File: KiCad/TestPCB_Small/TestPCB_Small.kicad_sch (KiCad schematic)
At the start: 82 parts, among them J2 USB4135-GF-A, Q1 SFH_3711, Q2 2N7002, Q3 2N7002, U1 ESP32-S3-WROOM-1, U1 MCP73831-2-OT, U2 TC1185-xCT, U4 LSM6DSM

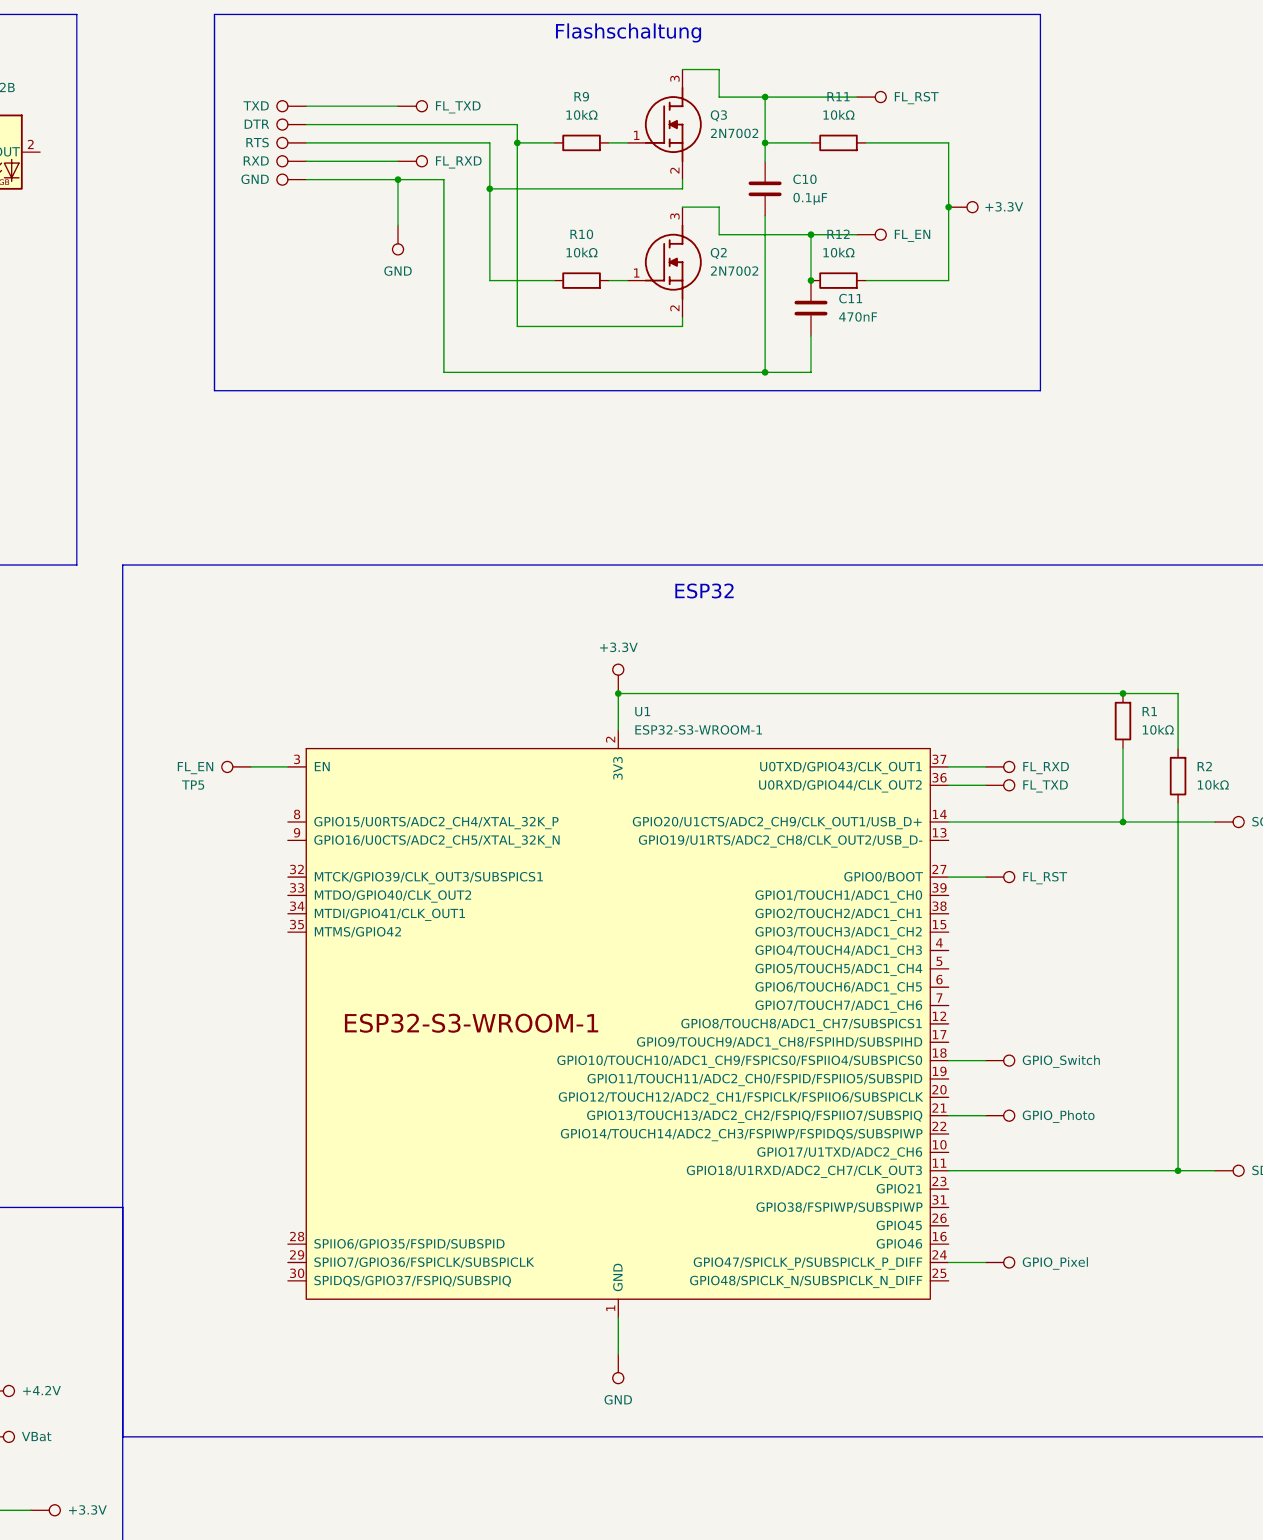
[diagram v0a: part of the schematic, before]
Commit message: CHG: pcb-layouts adopted
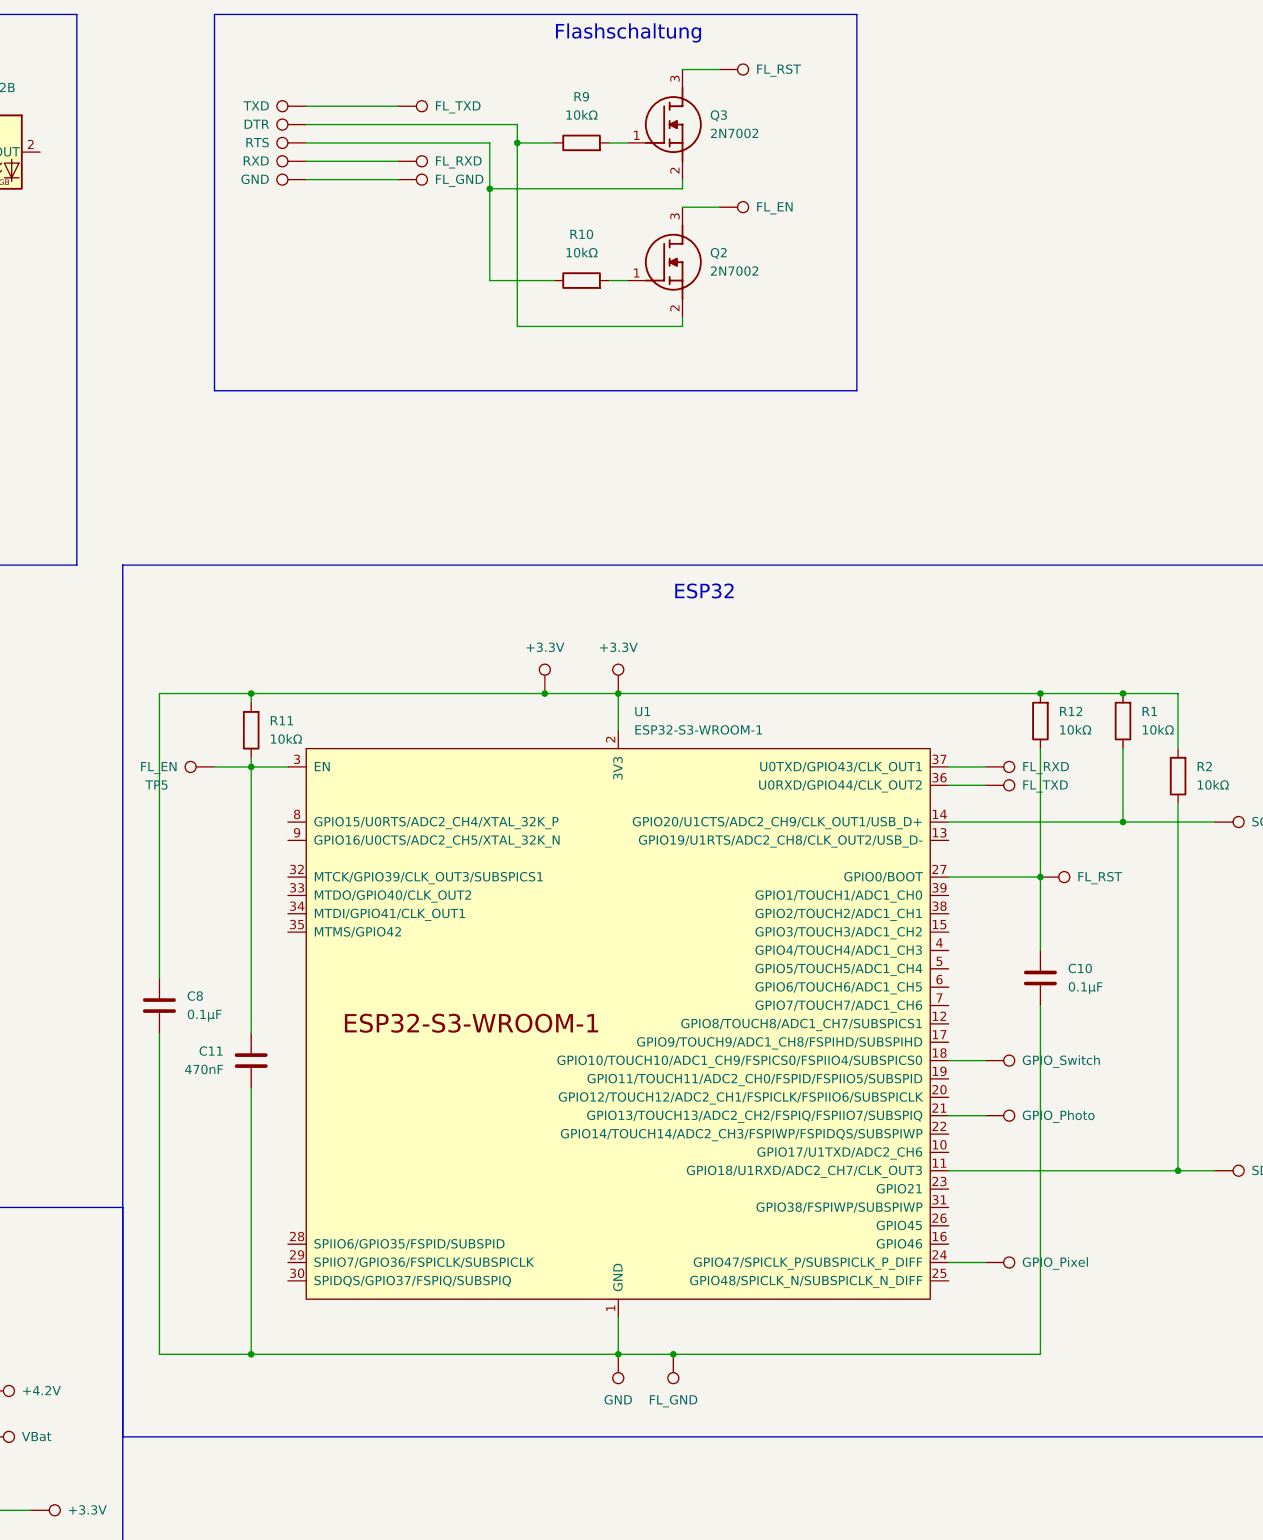
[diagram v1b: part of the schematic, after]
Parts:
- added C8: 0.1µF, Capacitor_SMD:C_0805_2012Metric, symbol Device:C
- added TP39: +3.3V, TestPoint:TestPoint_Pad_2.0x2.0mm, symbol Connector:TestPoint
- TP13: value GND -> FL_GND
- TP7: value +3.3V -> FL_GND
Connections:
- net at R11.2, R12.2: now also R1.2, R2.2, TP1.1, U1.2 (3V3), C8.1, TP39.1; no longer TP7.1
- net at Q2.3 (D), TP14.1: no longer C11.1, R12.1
- net at TP12.1, TP13.1: no longer C10.2, C11.2
- net at Q3.3 (D), TP17.1: no longer C10.1, R11.1
- net at TP6.1, U1.1 (GND), U1.40 (GND)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: now also C10.2, C11.2, TP7.1, C8.2
- net at TP4.1, U1.27 (GPIO0/BOOT): now also C10.1, R12.1
- net at TP5.1, U1.3 (EN): now also C11.1, R11.1
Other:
- moved on the sheet: C10, C11, R11, R12, TP5

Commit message: CHG: changes of today
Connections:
- net at S1.1: no longer TP29.1
- net at S1.4: now also TP29.1
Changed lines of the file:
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@@
+    (stroke (width 0) (type default))
+  )
+  (wire (pts (xy 158.75 130.81) (xy 162.56 130.81))
     (stroke (width 0) (type default))
   )
@@
   )
   (wire (pts (xy 368.3 127) (xy 368.3 144.78))
-    (stroke (width 0) (type default))
-  )
-  (wire (pts (xy 158.75 133.35) (xy 162.56 133.35))
     (stroke (width 0) (type default))
   )
@@
     )
   )
-  (symbol (lib_id "Connector:TestPoint") (at 158.75 133.35 90) (unit 1)
-    (in_bom yes) (on_board yes) (dnp no)
-    (property "Reference" "TP29" (at 153.67 134.62 90)
+  (symbol (lib_id "Connector:TestPoint") (at 158.75 130.81 90) (unit 1)
+    (in_bom yes) (on_board yes) (dnp no)
+    (property "Reference" "TP29" (at 153.67 132.08 90)
       (effects (font (size 1.27 1.27)) (justify left) hide)
     )
-    (property "Value" "GPIO_Switch" (at 153.67 133.35 90)
-      (effects (font (size 1.27 1.27)) (justify left))
-    )
-    (property "Footprint" "TestPoint:TestPoint_Pad_2.0x2.0mm" (at 158.75 128.27 0)
-      (effects (font (size 1.27 1.27)) hide)
-    )
-    (property "Datasheet" "~" (at 158.75 128.27 0)
-      (effects (font (size 1.27 1.27)) hide)
-    )
+    (property "Value" "GPIO_Switch" (at 153.67 130.81 90)
+      (effects (font (size 1.27 1.27)) (justify left))
+    )
+    (property "Footprint" "TestPoint:TestPoint_Pad_2.0x2.0mm" (at 158.75 125.73 0)
+      (effects (font (size 1.27 1.27)) hide)
+    )
+    (property "Datasheet" "~" (at 158.75 125.73 0)
+      (effects (font (size 1.27 1.27)) hide)
+    )
